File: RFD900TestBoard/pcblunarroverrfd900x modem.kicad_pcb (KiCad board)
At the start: 4 copper layers, 135 x 95 mm, 27 parts, among them J1 Barrel_Jack_Switch, J10 Conn_02x01, J11 Conn_02x01, J12 Conn_02x01, J13 Conn_02x01, J14 Conn_02x01, J16 Conn_02x01, J17 Conn_02x01, J18 Conn_01x11, J2 Conn_02x08_Counter_Clockwise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

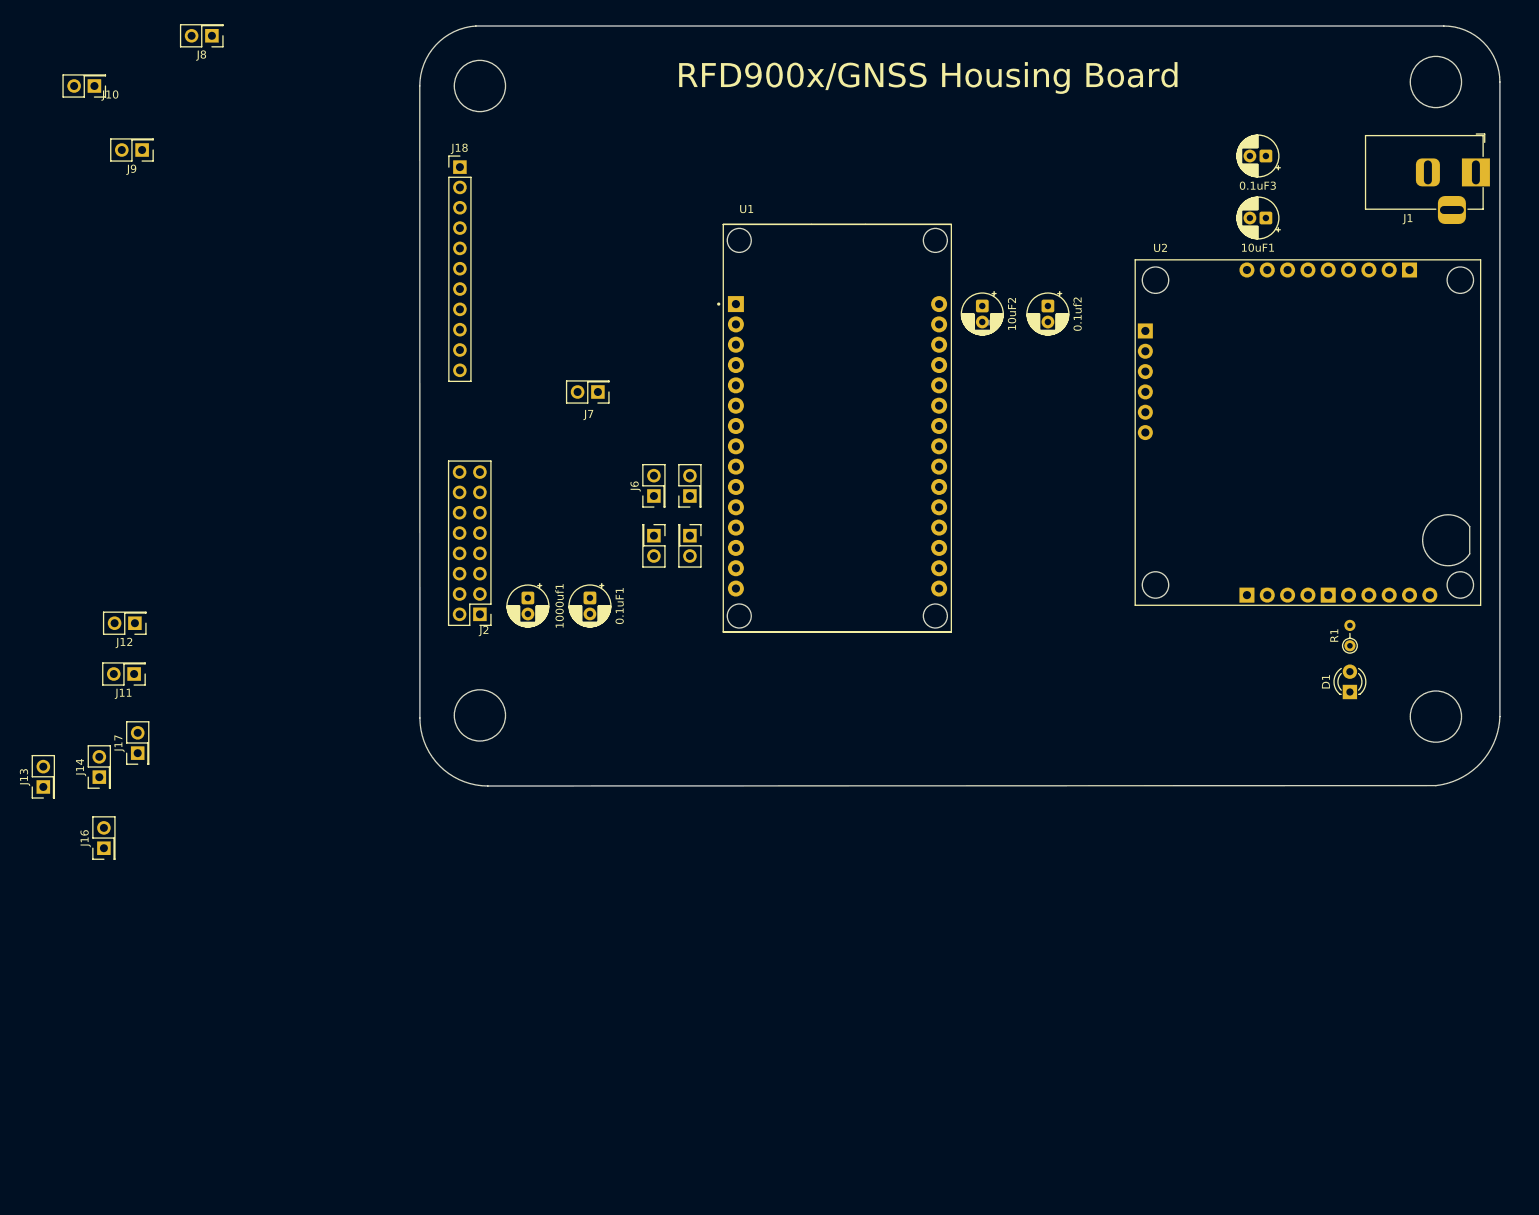
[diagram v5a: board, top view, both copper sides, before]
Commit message: made final changes to RFD900x Housing Board
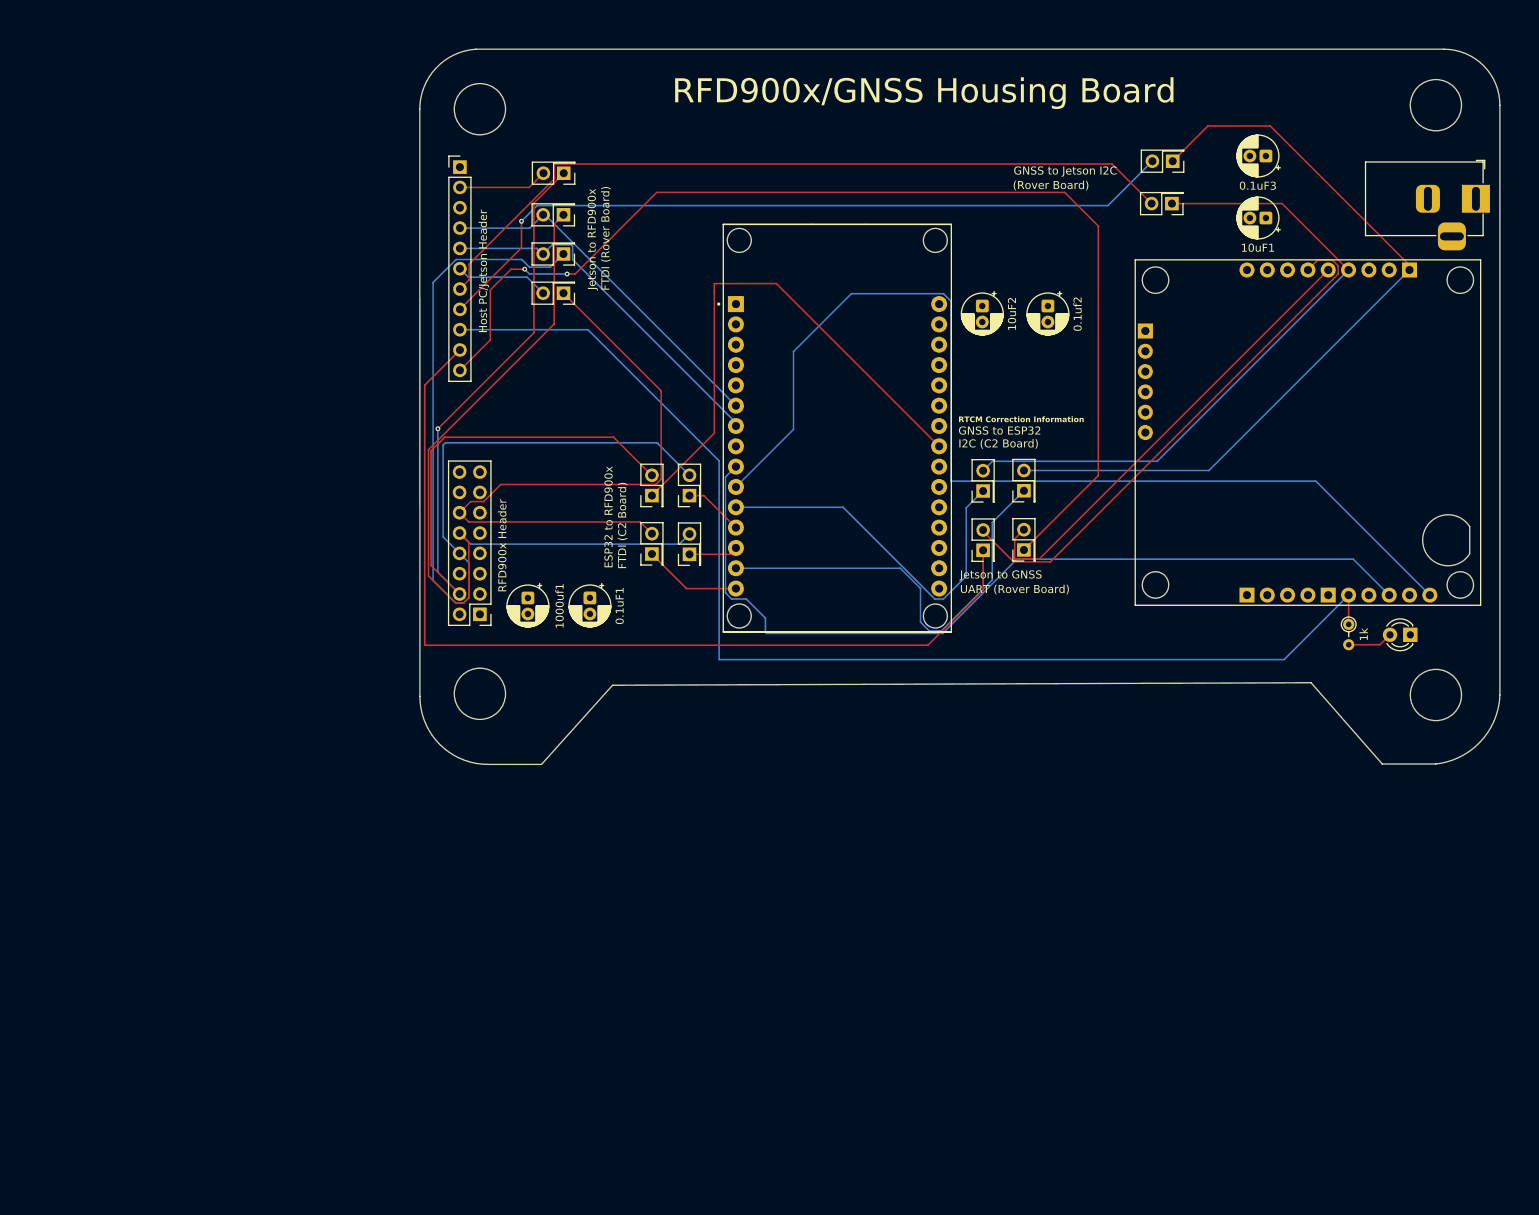
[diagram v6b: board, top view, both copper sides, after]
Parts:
- moved J11 142.4 mm to (164.0, 47.2)
- moved J12 142.0 mm to (164.1, 41.9)
- moved J13 128.0 mm to (145.5, 83.1)
- moved J14 116.1 mm to (140.4, 83.1)
- moved J16 116.0 mm to (140.4, 90.5)
- moved J17 113.6 mm to (145.5, 90.5)
- moved J10 59.7 mm to (88.0, 43.4)
- moved J9 53.3 mm to (87.9, 48.6)
- moved J8 51.7 mm to (87.9, 53.5)
- moved J7 13.1 mm to (87.9, 58.4)
- moved D1 10.4 mm to (193.8, 101.1), turned to 180 degrees
- moved J5 7.29 mm to (103.7, 91.0)
- moved J6 7.25 mm to (99.0, 91.0)
- moved J3 6.90 mm to (99.0, 83.7), turned to 90 degrees
- moved J4 6.70 mm to (103.7, 83.7), turned to 90 degrees
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- renumbered R1 to 1k
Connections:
- net RX renamed Net-(J2-Pin_8)
- net TX renamed Net-(J2-Pin_10)
- J10 pad 1: RTS -> Net-(J10-Pin_1)
- J2 pad 12: RTS -> Net-(J2-Pin_12)
- J2 pad 4: CTS -> Net-(J10-Pin_1)
- J3 pad 2: CTS -> Net-(J10-Pin_1)
- J6 pad 2: RTS -> Net-(J2-Pin_12)
- J7 pad 1: CTS -> Net-(J2-Pin_12)
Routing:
- net RTK-jet: track 0.00 -> 149.7 mm
- net TX2-jet: track 0.00 -> 139.3 mm, vias 0 -> 2
- net INT: track 0.00 -> 131.2 mm
- net RX2-jet: track 0.00 -> 116.3 mm
- net Net-(J2-Pin_8): track 0.00 -> 114.8 mm
- net Net-(J10-Pin_1): track 0.00 -> 109.9 mm, vias 0 -> 1
- net RST: track 0.00 -> 108.1 mm
- net Net-(J12-Pin_1): track 0.71 -> 98.5 mm
- net Net-(J2-Pin_10): track 0.00 -> 97.3 mm
- net SDA-jet: track 0.00 -> 97.2 mm
- net SCL-jet: track 0.00 -> 96.2 mm, vias 0 -> 1
- net Net-(J11-Pin_1): track 0.00 -> 81.6 mm
- net Net-(J2-Pin_12): track 0.00 -> 80.4 mm
- net Net-(J16-Pin_2): track 0.00 -> 66.6 mm
- net CTS-esp: track 0.00 -> 66.3 mm
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- added copper zone on In2.Cu, net +5V
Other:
- board size 135 x 95 mm -> 135 x 89.4 mm
- board text added: "(Rover Board)"
- board text added: "CTS"
- board text added: "ESP32 to RFD900x"
- board text added: "FTDI (C2 Board)"
- board text added: "FTDI (Rover Board)"
- board text added: "GND"
- board text added: "GNSS to ESP32"
- board text added: "GNSS to Jetson I2C"
- board text added: "Host PC/Jetson Header"
- board text added: "I2C (C2 Board)"
- board text added: "Jetson to GNSS"
- board text added: "Jetson to RFD900x"
- board text added: "RFD900x Header"
- board text added: "RTCM Correction Information"
- board text added: "RTK"
- board text added: "RTS"
- board text added: "RX1"
- board text added: "RX2"
- board text added: "SCL"
- board text added: "SDA"
- board text added: "TX1"
- board text added: "TX2"
- board text added: "UART (Rover Board)"

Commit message: hello!!!!!!!!
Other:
- board text added: "Aden Briano Lord Aayan Ilyas the 2nd"
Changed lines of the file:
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@@
+		)
+	)
+	(gr_text "Aden Briano\nLord Aayan Ilyas the 2nd"
+		(at 102.7 38.2 0)
+		(layer "B.SilkS")
+		(effects
+			(font
+				(size 1 1)
+				(thickness 0.1)
+			)
+			(justify left bottom mirror)
 		)
 	)
